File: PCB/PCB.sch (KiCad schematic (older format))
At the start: 2 parts

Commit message: Schema presque terminé
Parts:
- removed D?: ZPDxx, Diode_THT:D_DO-35_SOD27_P10.16mm_Horizontal, symbol Diode:ZPDxx
- removed Q?: 2N2222, symbol Device:Q_NPN_EBC
- added C? (x2): CP, symbol Device:CP
- added C? (x4): C, symbol Device:C
- added D?: D_Zener, symbol Device:D_Zener
- added HS? (x2): Heatsink, symbol Mechanical:Heatsink
- added Q? (x5): 2N2907, symbol Device:Q_PNP_EBC
- added Q? (x2): BD139, symbol Device:Q_NPN_ECB
- added Q? (x2): 2N2222, symbol Device:Q_NPN_EBC
- added Q?: TIP32, symbol Device:Q_PNP_BCE
- added Q?: BD138, symbol Device:Q_PNP_ECB
- added Q?: Q_NPN_BCE, symbol Device:Q_NPN_BCE
- added R? (x15): R, symbol Device:R
- added RV? (x2): R_POT, symbol Device:R_POT
- added U?: Jack_Mono, symbol CmpAmpliAudio:Jack_Mono
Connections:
- net labels added: +12V, -12V, GND

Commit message: placement quasi fini
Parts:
- added C3: CP, symbol Device:CP
- added D1, D2: 1N4148, Diode_THT:D_DO-35_SOD27_P7.62mm_Horizontal, symbol Diode:1N4148
- added J2: Conn_01x02, symbol Connector_Generic:Conn_01x02
- added K?: ADW11, Relay_THT:Relay_1P1T_NO_10x24x18.8mm_Panasonic_ADW11xxxxW_THT, symbol Relay:ADW11
- added Q13: 2N2222, symbol Device:Q_NPN_EBC
- added R16, R17: R, symbol Device:R
- C11: renamed from C?; value C -> C11
- Dz1: renamed from D?; value D_Zener -> BZX55C5V1
- Q12: renamed from Q?; value Q_NPN_BCE -> TIP31
- gave numbers to parts that had none: 36
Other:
- moved on the sheet: C10, C11

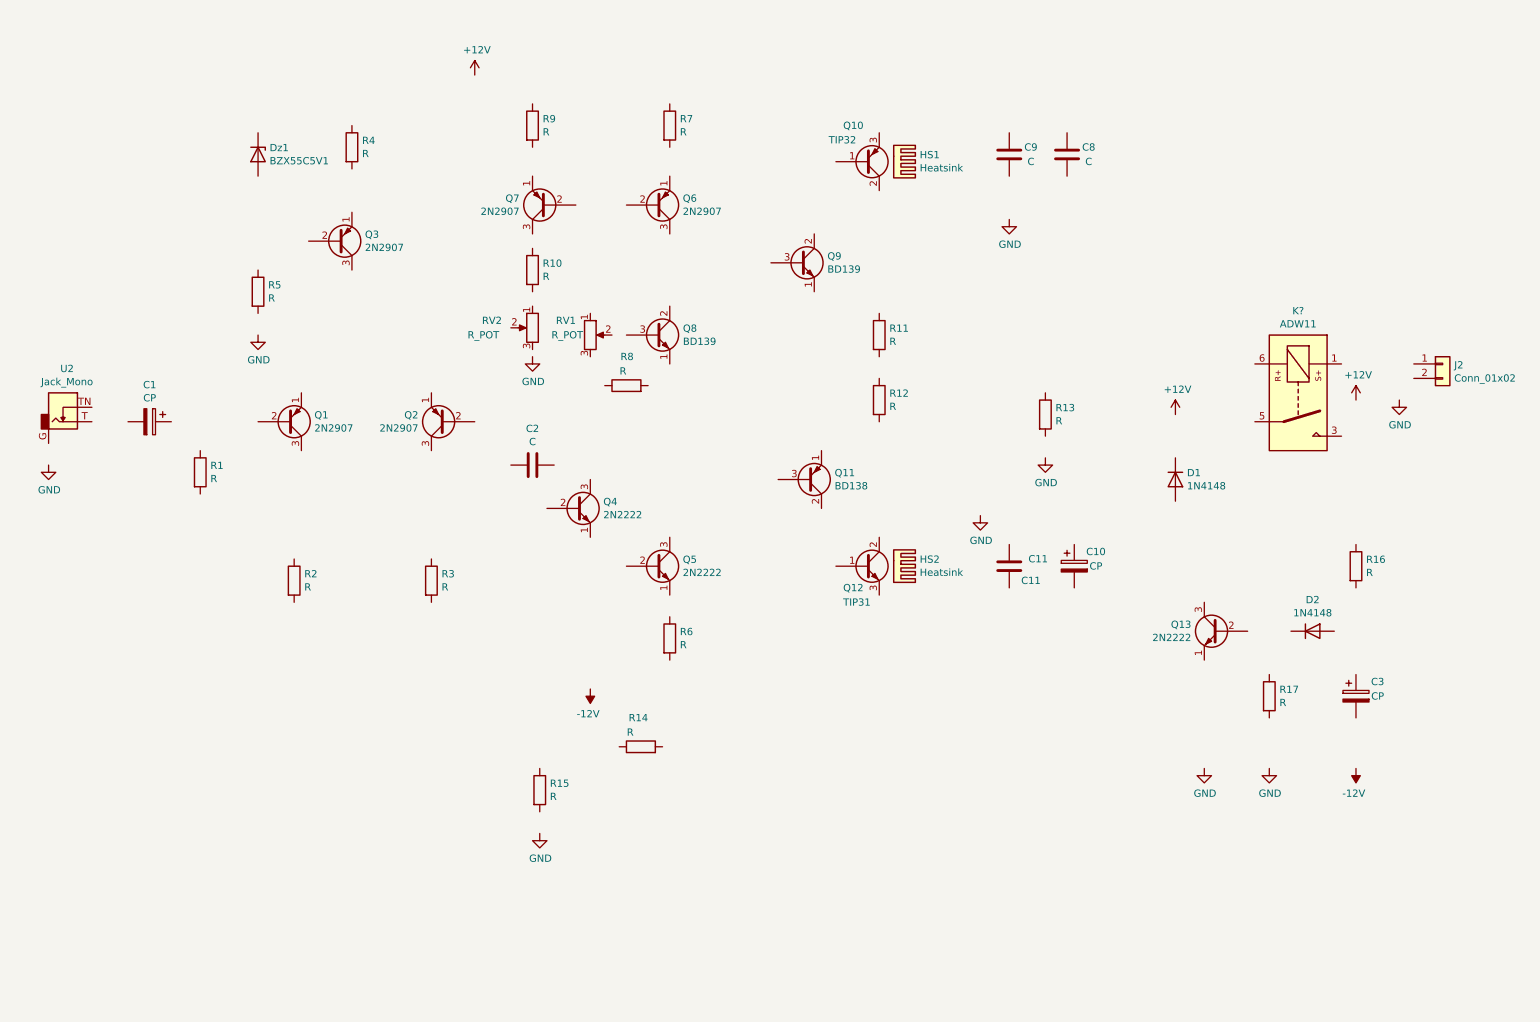
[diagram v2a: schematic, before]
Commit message: schema termine sauf relai
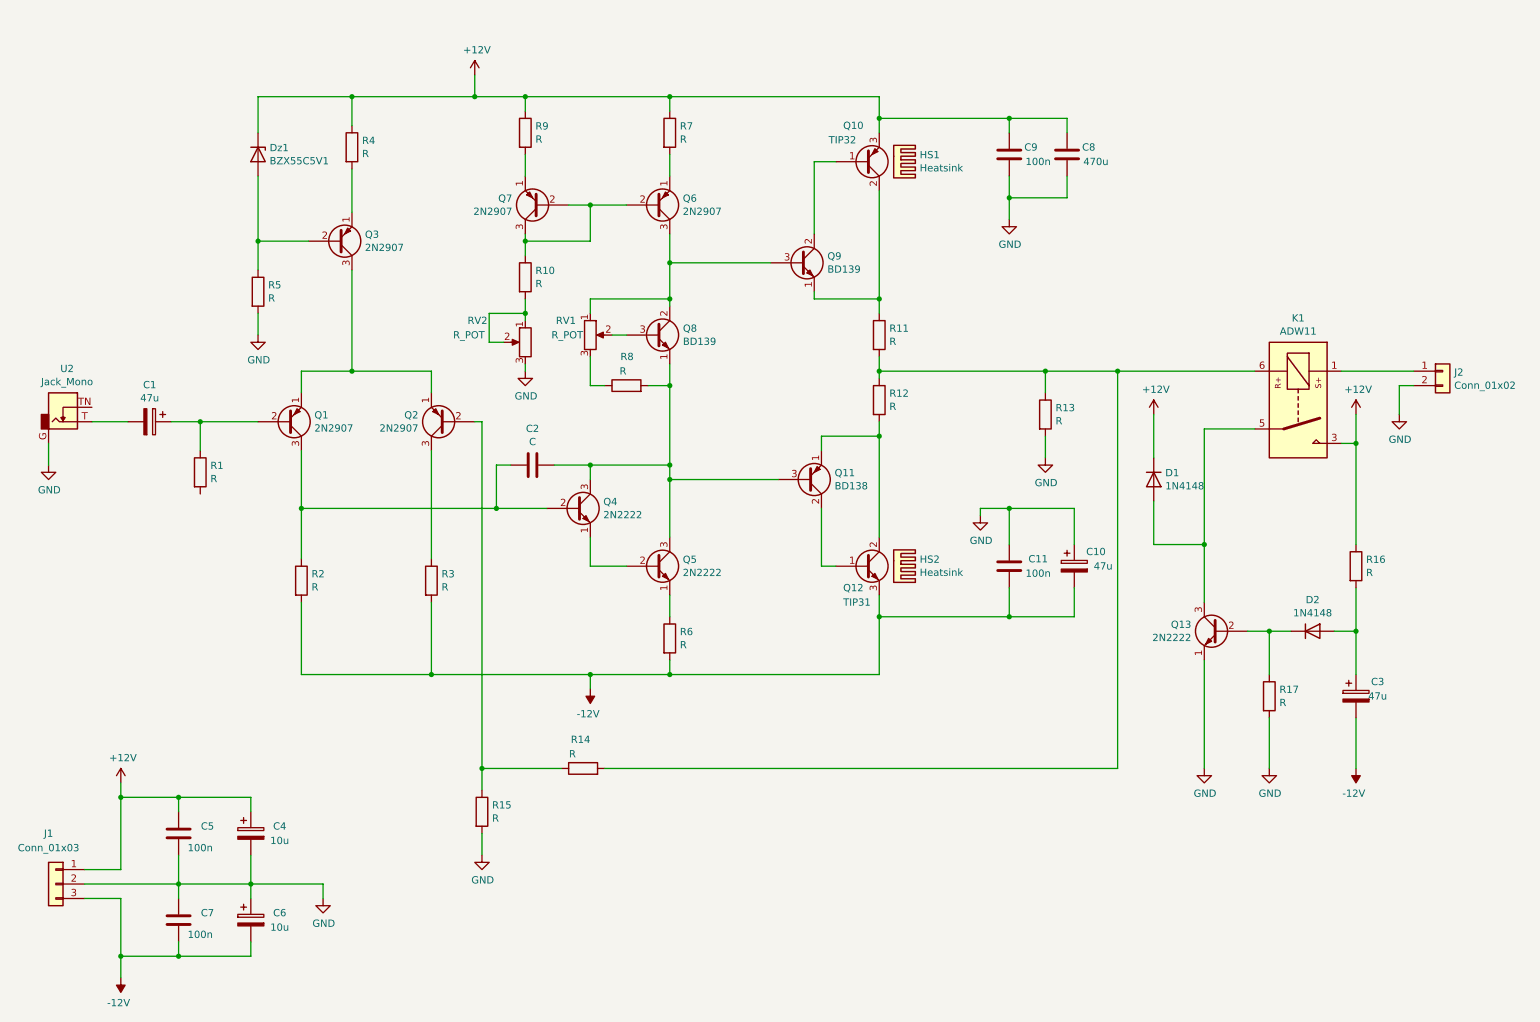
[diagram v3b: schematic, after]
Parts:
- added C4, C6: 10u, symbol Device:CP
- added C5, C7: 100n, symbol Device:C
- added J1: Conn_01x03, symbol Connector_Generic:Conn_01x03
- C1, C10, C3: value CP -> 47u
- C11: value C11 -> 100n
- C8: value C -> 470u
- C9: value C -> 100n
- gave numbers to parts that had none: 1
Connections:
- net +12V: now also C8.1, C9.1, D1.1 (K), Dz1.1 (K), K1.3, Q10.3 (E), R16.1, R4.1, R7.1, R9.1, C4.1, C5.1, J1.1 (Pin_1)
- net -12V: now also C10.2, C11.2, C3.2, Q12.3 (E), R2.2, R3.2, R6.2, C6.2, C7.2, J1.3 (Pin_3)
- net GND: now also C10.1, C11.1, C8.2, C9.2, J2.2 (Pin_2), Q13.1 (E), R13.2, R15.2, R17.2, R5.2, RV2.3, U2.G, C4.2, C5.2, C6.1, C7.1, J1.2 (Pin_2)
- net at Dz1.2 (A): now also Q3.2 (B), R5.1
- net at R4.2: now also Q3.1 (E)
- net at Q1.1 (E): now also Q2.1 (E), Q3.3 (C)
- net at Q1.2 (B): now also C1.1, R1.1
- net at Q1.3 (C): now also C2.2, Q4.2 (B), R2.1
- net at Q2.2 (B): now also R14.1, R15.1
- net at Q2.3 (C): now also R3.1
- net at C1.2: now also U2.T
- net at R14.2: now also K1.6, R11.2, R12.1, R13.1
- net at D1.2 (A): now also K1.5, Q13.3 (C)
- net at R9.2: now also Q7.1 (E)
- net at R7.2: now also Q6.1 (E)
- net at Q6.2 (B): now also Q7.2 (B), Q7.3 (C), R10.1
- net at Q6.3 (C): now also Q8.2 (C), Q9.3 (B), RV1.1
- net at R10.2: now also RV2.1, RV2.2
- net at K1.1: now also J2.1 (Pin_1)
- net at Q8.1 (E): now also C2.1, Q11.3 (B), Q4.3 (C), Q5.3 (C), R8.2
- net at Q8.3 (B): now also RV1.2
- net at RV1.3: now also R8.1
- net at R16.2: now also C3.1, D2.2 (A)
- net at D2.1 (K): now also Q13.2 (B), R17.1
- net at Q5.1 (E): now also R6.1
- net at Q5.2 (B): now also Q4.1 (E)
- net at Q10.1 (B): now also Q9.2 (C)
- net at Q10.2 (C): now also Q9.1 (E), R11.1
- net at R12.2: now also Q11.1 (E), Q12.2 (C)
- net at Q11.2 (C): now also Q12.1 (B)
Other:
- moved on the sheet: D1, J2, K1, Q7, R10, R14, R15, R2, R7, R9, RV2

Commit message: schema fini
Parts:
- removed K1: ADW11, Relay_THT:Relay_1P1T_NO_10x24x18.8mm_Panasonic_ADW11xxxxW_THT, symbol Relay:ADW11
- added U11: Relai, symbol CMP_Relai:Relai
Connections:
- net +12V: now also U11.b2
- net GND: now also R1.2
- net at R11.2, R12.1, R13.1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: now also U11.c1
- net at D1.2 (A), Q13.3 (C): now also U11.b1
- net at J2.1 (Pin_1): now also U11.c2
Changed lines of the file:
@@
-$EndComp
-$Comp
-L Relay:ADW11 K1
-U 1 1 605C0AEB
-P 9600 3250
-F 0 "K1" V 9033 3250 50  0000 C CNN
-F 1 "ADW11" V 9124 3250 50  0000 C CNN
-F 2 "Relay_THT:Relay_1P1T_NO_10x24x18.8mm_Panasonic_ADW11xxxxW_THT" H 10925 3200 50  0001 C CNN
-F 3 "https://www.panasonic-electric-works.com/pew/es/downloads/ds_dw_hl_en.pdf" H 9600 3250 50  0001 C CNN
-	1    9600 3250
-	0    1    1    0
 $EndComp
 $Comp
@@
 	10300 3150 10400 3150
 Wire Wire Line
-	9900 3550 10000 3550
-Wire Wire Line
-	10000 3550 10000 4250
-Wire Wire Line
 	9850 4850 10000 4850
 Wire Wire Line
@@
 	1    0    0    -1
 $EndComp
-Wire Wire Line
-	10000 3550 10000 3350
-Connection ~ 10000 3550
 Wire Wire Line
 	8950 5050 8950 5800
@@
 Wire Wire Line
 	2350 6600 2350 6700
+$Comp
+L CMP_Relai:Relai U11
+U 1 1 6061B877
+P 9650 3150
+F 0 "U11" H 9600 3517 50  0000 C CNN
+F 1 "Relai" H 9600 3426 50  0000 C CNN
+F 2 "" V 9250 3000 50  0001 C CNN
+F 3 "" V 9250 3000 50  0001 C CNN
+	1    9650 3150
+	1    0    0    -1
+$EndComp
+Wire Wire Line
+	9900 3450 10000 3450
+Wire Wire Line
+	10000 3350 10000 3450
+Connection ~ 10000 3450
+Wire Wire Line
+	10000 3450 10000 4250
+$Comp
+L power:GND #PWR0101
+U 1 1 6061B973
+P 2000 3900
+F 0 "#PWR0101" H 2000 3650 50  0001 C CNN
+F 1 "GND" H 2005 3727 50  0000 C CNN
+F 2 "" H 2000 3900 50  0001 C CNN
+F 3 "" H 2000 3900 50  0001 C CNN
+	1    2000 3900
+	1    0    0    -1
+$EndComp
 $EndSCHEMATC

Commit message: tout debut empreinte
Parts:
- C1, C10, C3: footprint (none) -> CmpAmpliAudio:CP_Radial_D8.0mm_P5.00mm
- C11, C2, C5, C7, C9: footprint (none) -> CmpAmpliAudio:C_Rect_L7.2mm_W3.5mm_P5.00mm_FKS2_FKP2_MKS2_MKP2
- D1, D2: footprint Diode_THT:D_DO-35_SOD27_P7.62mm_Horizontal -> CmpAmpliAudio:D_DO-35_SOD27_P10.16mm_Horizontal
- Dz1: footprint (none) -> CmpAmpliAudio:D_DO-35_SOD27_P10.16mm_Horizontal
- HS1, HS2: footprint (none) -> CmpAmpliAudio:Heatsink_Fischer_SK104-STC-STIC_35x13mm_2xDrill2.5mm
- J1: footprint (none) -> CmpAmpliAudio:PhoenixContact_MSTBVA_2,5_3-G-5,08_1x03_P5.08mm_Vertical
- J2: footprint (none) -> CmpAmpliAudio:PhoenixContact_MSTBVA_2,5_2-G-5,08_1x02_P5.08mm_Vertical
- Q1, Q13, Q2, Q3, Q4, Q5, Q6, Q7: footprint (none) -> CmpAmpliAudio:TO-18-3
- Q10, Q12: footprint (none) -> CmpAmpliAudio:TO-220-3_Vertical
- Q11, Q8, Q9: footprint (none) -> CmpAmpliAudio:TO-126-3_Vertical
- U2: footprint (none) -> CmpAmpliAudio:Jack_35RAPC2AV
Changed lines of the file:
@@
 F 0 "Dz1" V 2354 1630 50  0000 L CNN
 F 1 "BZX55C5V1" V 2445 1630 50  0000 L CNN
-F 2 "" H 2400 1550 50  0001 C CNN
+F 2 "CmpAmpliAudio:D_DO-35_SOD27_P10.16mm_Horizontal" H 2400 1550 50  0001 C CNN
 F 3 "~" H 2400 1550 50  0001 C CNN
 	1    2400 1550
@@
 F 0 "Q1" H 2790 3354 50  0000 L CNN
 F 1 "2N2907" H 2790 3445 50  0000 L CNN
-F 2 "" H 2800 3500 50  0001 C CNN
+F 2 "CmpAmpliAudio:TO-18-3" H 2800 3500 50  0001 C CNN
 F 3 "~" H 2600 3400 50  0001 C CNN
 	1    2600 3400
@@
 F 0 "Q3" H 3140 2104 50  0000 L CNN
 F 1 "2N2907" H 3140 2195 50  0000 L CNN
-F 2 "" H 3150 2250 50  0001 C CNN
+F 2 "CmpAmpliAudio:TO-18-3" H 3150 2250 50  0001 C CNN
 F 3 "~" H 2950 2150 50  0001 C CNN
 	1    2950 2150
@@
 F 0 "C1" V 1395 3400 50  0000 C CNN
 F 1 "47u" V 1486 3400 50  0000 C CNN
-F 2 "" H 1688 3250 50  0001 C CNN
+F 2 "CmpAmpliAudio:CP_Radial_D8.0mm_P5.00mm" H 1688 3250 50  0001 C CNN
 F 3 "~" H 1650 3400 50  0001 C CNN
 	1    1650 3400
@@
 F 0 "U2" H 1078 3567 50  0000 C CNN
 F 1 "Jack_Mono" H 1078 3476 50  0000 C CNN
-F 2 "" H 1100 3500 50  0001 C CNN
+F 2 "CmpAmpliAudio:Jack_35RAPC2AV" H 1100 3500 50  0001 C CNN
 F 3 "" H 1100 3500 50  0001 C CNN
 	1    1050 3300
@@
 F 0 "Q6" H 5340 1854 50  0000 L CNN
 F 1 "2N2907" H 5340 1945 50  0000 L CNN
-F 2 "" H 5350 2000 50  0001 C CNN
+F 2 "CmpAmpliAudio:TO-18-3" H 5350 2000 50  0001 C CNN
 F 3 "~" H 5150 1900 50  0001 C CNN
 	1    5150 1900
@@
 F 0 "Q8" H 5341 2846 50  0000 L CNN
 F 1 "BD139" H 5341 2755 50  0000 L CNN
-F 2 "" H 5350 2900 50  0001 C CNN
+F 2 "CmpAmpliAudio:TO-126-3_Vertical" H 5350 2900 50  0001 C CNN
 F 3 "~" H 5150 2800 50  0001 C CNN
 	1    5150 2800
@@
 F 0 "Q7" H 4540 1854 50  0000 L CNN
 F 1 "2N2907" H 4540 1945 50  0000 L CNN
-F 2 "" H 4550 2000 50  0001 C CNN
+F 2 "CmpAmpliAudio:TO-18-3" H 4550 2000 50  0001 C CNN
 F 3 "~" H 4350 1900 50  0001 C CNN
 	1    4350 1900
@@
 F 0 "Q5" H 5340 4446 50  0000 L CNN
 F 1 "2N2222" H 5340 4355 50  0000 L CNN
-F 2 "" H 5350 4500 50  0001 C CNN
+F 2 "CmpAmpliAudio:TO-18-3" H 5350 4500 50  0001 C CNN
 F 3 "~" H 5150 4400 50  0001 C CNN
 	1    5150 4400
@@
 F 0 "Q4" H 4790 4046 50  0000 L CNN
 F 1 "2N2222" H 4790 3955 50  0000 L CNN
-F 2 "" H 4800 4100 50  0001 C CNN
+F 2 "CmpAmpliAudio:TO-18-3" H 4800 4100 50  0001 C CNN
 F 3 "~" H 4600 4000 50  0001 C CNN
 	1    4600 4000
@@
 F 0 "C2" V 4048 3700 50  0000 C CNN
 F 1 "C" V 4139 3700 50  0000 C CNN
-F 2 "" H 4338 3550 50  0001 C CNN
+F 2 "CmpAmpliAudio:C_Rect_L7.2mm_W3.5mm_P5.00mm_FKS2_FKP2_MKS2_MKP2" H 4338 3550 50  0001 C CNN
 F 3 "~" H 4300 3700 50  0001 C CNN
 	1    4300 3700
@@
 F 0 "Q10" H 6450 1350 50  0000 L CNN
 F 1 "TIP32" H 6350 1450 50  0000 L CNN
-F 2 "" H 6800 1700 50  0001 C CNN
+F 2 "CmpAmpliAudio:TO-220-3_Vertical" H 6800 1700 50  0001 C CNN
 F 3 "~" H 6600 1600 50  0001 C CNN
 	1    6600 1600
@@
 F 0 "Q9" H 6341 2346 50  0000 L CNN
 F 1 "BD139" H 6341 2255 50  0000 L CNN
-F 2 "" H 6350 2400 50  0001 C CNN
+F 2 "CmpAmpliAudio:TO-126-3_Vertical" H 6350 2400 50  0001 C CNN
 F 3 "~" H 6150 2300 50  0001 C CNN
 	1    6150 2300
@@
 F 0 "C9" H 7750 1600 50  0000 C CNN
 F 1 "100n" H 7800 1500 50  0000 C CNN
-F 2 "" H 7638 1400 50  0001 C CNN
+F 2 "CmpAmpliAudio:C_Rect_L7.2mm_W3.5mm_P5.00mm_FKS2_FKP2_MKS2_MKP2" H 7638 1400 50  0001 C CNN
 F 3 "~" H 7600 1550 50  0001 C CNN
 	1    7600 1550
@@
 F 0 "HS1" V 6753 1780 50  0000 L CNN
 F 1 "Heatsink" V 6844 1780 50  0000 L CNN
-F 2 "" H 6812 1600 50  0001 C CNN
+F 2 "CmpAmpliAudio:Heatsink_Fischer_SK104-STC-STIC_35x13mm_2xDrill2.5mm" H 6812 1600 50  0001 C CNN
 F 3 "~" H 6812 1600 50  0001 C CNN
 	1    6800 1600
@@
 F 0 "Q11" H 6391 3754 50  0000 L CNN
 F 1 "BD138" H 6391 3845 50  0000 L CNN
-F 2 "" H 6400 3900 50  0001 C CNN
+F 2 "CmpAmpliAudio:TO-126-3_Vertical" H 6400 3900 50  0001 C CNN
 F 3 "~" H 6200 3800 50  0001 C CNN
 	1    6200 3800
@@
 F 0 "Q12" H 6450 4250 50  0000 L CNN
 F 1 "TIP31" H 6450 4150 50  0000 L CNN
-F 2 "" H 6800 4500 50  0001 C CNN
+F 2 "CmpAmpliAudio:TO-220-3_Vertical" H 6800 4500 50  0001 C CNN
 F 3 "~" H 6600 4400 50  0001 C CNN
 	1    6600 4400
@@
 F 0 "HS2" V 6753 4580 50  0000 L CNN
 F 1 "Heatsink" V 6844 4580 50  0000 L CNN
-F 2 "" H 6812 4400 50  0001 C CNN
+F 2 "CmpAmpliAudio:Heatsink_Fischer_SK104-STC-STIC_35x13mm_2xDrill2.5mm" H 6812 4400 50  0001 C CNN
 F 3 "~" H 6812 4400 50  0001 C CNN
 	1    6800 4400
@@
 F 0 "D1" V 8554 3880 50  0000 L CNN
 F 1 "1N4148" V 8645 3880 50  0000 L CNN
-F 2 "Diode_THT:D_DO-35_SOD27_P7.62mm_Horizontal" H 8600 3625 50  0001 C CNN
+F 2 "CmpAmpliAudio:D_DO-35_SOD27_P10.16mm_Horizontal" H 8600 3625 50  0001 C CNN
 F 3 "https://assets.nexperia.com/documents/data-sheet/1N4148_1N4448.pdf" H 8600 3800 50  0001 C CNN
 	1    8600 3800
@@
 F 0 "J2" H 10680 3042 50  0000 L CNN
 F 1 "Conn_01x02" H 10680 2951 50  0000 L CNN
-F 2 "" H 10600 3050 50  0001 C CNN
+F 2 "CmpAmpliAudio:PhoenixContact_MSTBVA_2,5_2-G-5,08_1x02_P5.08mm_Vertical" H 10600 3050 50  0001 C CNN
 F 3 "~" H 10600 3050 50  0001 C CNN
 	1    10600 3050
@@
 F 0 "D2" H 9700 5067 50  0000 C CNN
 F 1 "1N4148" H 9700 4976 50  0000 C CNN
-F 2 "Diode_THT:D_DO-35_SOD27_P7.62mm_Horizontal" H 9700 4675 50  0001 C CNN
+F 2 "CmpAmpliAudio:D_DO-35_SOD27_P10.16mm_Horizontal" H 9700 4675 50  0001 C CNN
 F 3 "https://assets.nexperia.com/documents/data-sheet/1N4148_1N4448.pdf" H 9700 4850 50  0001 C CNN
 	1    9700 4850
@@
 F 0 "Q13" H 9240 4896 50  0000 L CNN
 F 1 "2N2222" H 9240 4805 50  0000 L CNN
-F 2 "" H 9250 4950 50  0001 C CNN
+F 2 "CmpAmpliAudio:TO-18-3" H 9250 4950 50  0001 C CNN
 F 3 "~" H 9050 4850 50  0001 C CNN
 	1    9050 4850
@@
 F 0 "C10" H 8200 4500 50  0000 C CNN
 F 1 "47u" H 8250 4400 50  0000 C CNN
-F 2 "" H 8088 4250 50  0001 C CNN
+F 2 "CmpAmpliAudio:CP_Radial_D8.0mm_P5.00mm" H 8088 4250 50  0001 C CNN
 F 3 "~" H 8050 4400 50  0001 C CNN
 	1    8050 4400
@@
 F 0 "C3" H 10150 5400 50  0000 C CNN
 F 1 "47u" H 10150 5300 50  0000 C CNN
-F 2 "" H 10038 5150 50  0001 C CNN
+F 2 "CmpAmpliAudio:CP_Radial_D8.0mm_P5.00mm" H 10038 5150 50  0001 C CNN
 F 3 "~" H 10000 5300 50  0001 C CNN
 	1    10000 5300
@@
 F 0 "J1" H 1050 6950 50  0000 C CNN
 F 1 "Conn_01x03" H 1050 6850 50  0000 C CNN
-F 2 "" H 1000 6600 50  0001 C CNN
+F 2 "CmpAmpliAudio:PhoenixContact_MSTBVA_2,5_3-G-5,08_1x03_P5.08mm_Vertical" H 1000 6600 50  0001 C CNN
 F 3 "~" H 1000 6600 50  0001 C CNN
 	1    1000 6600
@@
 F 0 "C11" H 7800 4450 50  0000 C CNN
 F 1 "100n" H 7800 4350 50  0000 C CNN
-F 2 "" H 7638 4250 50  0001 C CNN
+F 2 "CmpAmpliAudio:C_Rect_L7.2mm_W3.5mm_P5.00mm_FKS2_FKP2_MKS2_MKP2" H 7638 4250 50  0001 C CNN
 F 3 "~" H 7600 4400 50  0001 C CNN
 	1    7600 4400
@@
 F 0 "C5" H 2050 6300 50  0000 C CNN
 F 1 "100n" H 2000 6150 50  0000 C CNN
-F 2 "" H 1888 6100 50  0001 C CNN
+F 2 "CmpAmpliAudio:C_Rect_L7.2mm_W3.5mm_P5.00mm_FKS2_FKP2_MKS2_MKP2" H 1888 6100 50  0001 C CNN
 F 3 "~" H 1850 6250 50  0001 C CNN
 	1    1850 6250
@@
 F 0 "C7" H 2050 6900 50  0000 C CNN
 F 1 "100n" H 2000 6750 50  0000 C CNN
-F 2 "" H 1888 6700 50  0001 C CNN
+F 2 "CmpAmpliAudio:C_Rect_L7.2mm_W3.5mm_P5.00mm_FKS2_FKP2_MKS2_MKP2" H 1888 6700 50  0001 C CNN
 F 3 "~" H 1850 6850 50  0001 C CNN
 	1    1850 6850
@@
 F 0 "Q2" H 3890 3354 50  0000 L CNN
 F 1 "2N2907" H 3890 3445 50  0000 L CNN
-F 2 "" H 3900 3500 50  0001 C CNN
+F 2 "CmpAmpliAudio:TO-18-3" H 3900 3500 50  0001 C CNN
 F 3 "~" H 3700 3400 50  0001 C CNN
 	1    3700 3400
